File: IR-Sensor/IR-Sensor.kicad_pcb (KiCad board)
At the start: 2 copper layers, 11 parts, among them J1 Conn_01x03_Male, U1 LM324

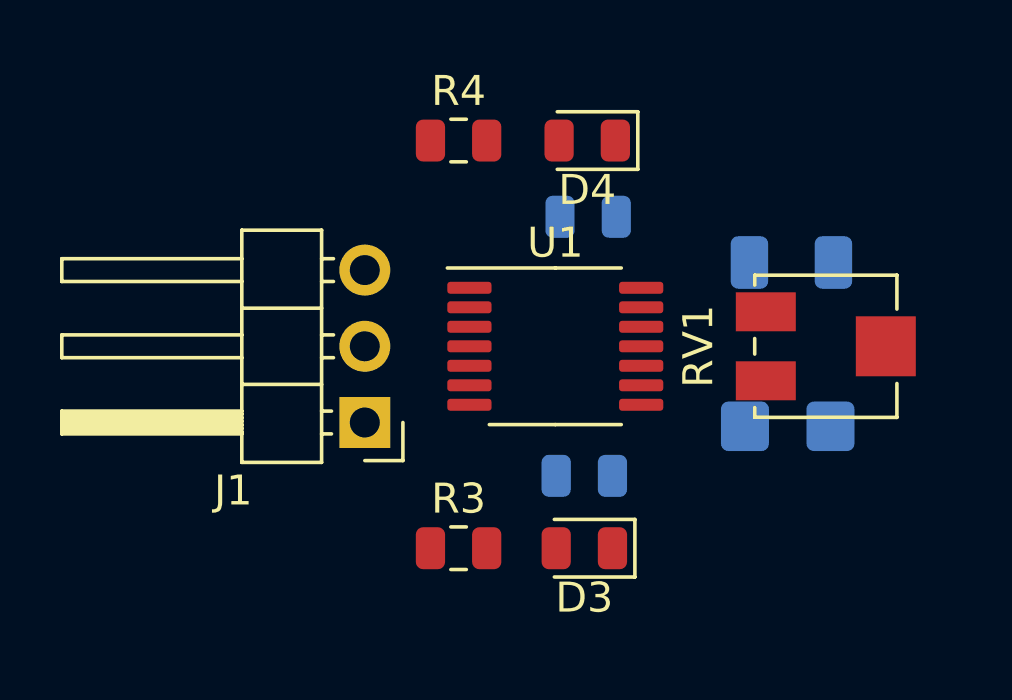
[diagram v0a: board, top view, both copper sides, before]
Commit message: Added edge cuts
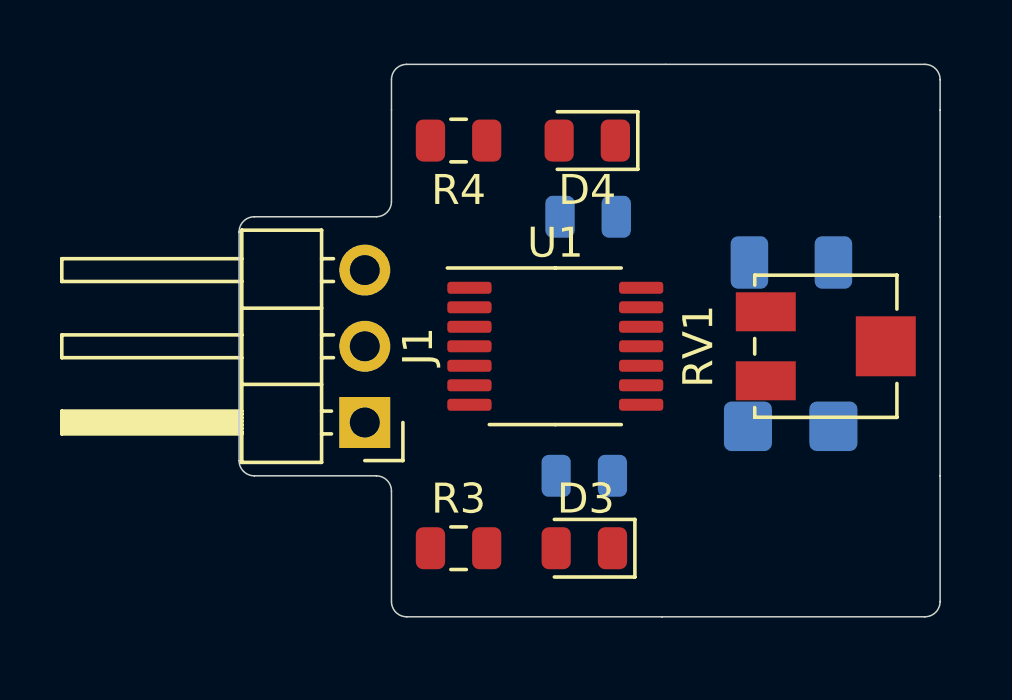
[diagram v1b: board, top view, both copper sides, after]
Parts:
- moved D2 0.10 mm to (134.3, 83.1)
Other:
- board outline added: 23.4 x 18.4 mm

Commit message: Added connections
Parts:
- turned D1 to 180 degrees
- turned D2 to 180 degrees
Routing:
- net VCC: track 0.00 -> 31.3 mm, vias 0 -> 1
- net Net-(RV1-Pad2): track 0.00 -> 19.7 mm
- net /OUTPUT: track 0.00 -> 19.6 mm, vias 0 -> 2
- net Net-(D2-Pad2): track 0.00 -> 16.8 mm, vias 0 -> 1
- net Net-(D1-Pad2): track 0.00 -> 5.07 mm
- net Net-(D4-Pad2): track 0.00 -> 2.41 mm
- net Net-(D3-Pad2): track 0.00 -> 2.32 mm
- added copper zone on B.Cu, net GND
- added copper zone on F.Cu, net GND
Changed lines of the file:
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@@
   (general
     (thickness 1.6)
-    (drawings 35)
-    (tracks 0)
+    (drawings 36)
+    (tracks 56)
     (zones 0)
     (modules 11)
@@
     (38 B.Mask user)
     (39 F.Mask user)
-    (40 Dwgs.User user)
+    (40 Dwgs.User user hide)
     (41 Cmts.User user)
     (42 Eco1.User user)
@@
   )
   (module LED_SMD:LED_1206_3216Metric (layer B.Cu)
-    (at 134.363 77.597)
+    (at 134.363 77.597 180)
     (descr "LED SMD 1206 (3216 Metric), square (rectangular) end terminal, IPC_7351 nominal, (Body size source: http://www.tortai-tech.com/upload/download/2011102023233369053.pdf), generated with kicad-footprint-generator")
     (tags diode)
@@
       (effects (font (size 0.8 0.8) (thickness 0.12)) (justify mirror))
     )
-    (pad 1 smd roundrect (at -1.4 0) (size 1.25 1.75) (layers B.Cu B.Paste B.Mask) (roundrect_rratio 0.2)
+    (pad 1 smd roundrect (at -1.4 0 180) (size 1.25 1.75) (layers B.Cu B.Paste B.Mask) (roundrect_rratio 0.2)
       (net 1 GND))
-    (pad 2 smd roundrect (at 1.4 0) (size 1.25 1.75) (layers B.Cu B.Paste B.Mask) (roundrect_rratio 0.2)
+    (pad 2 smd roundrect (at 1.4 0 180) (size 1.25 1.75) (layers B.Cu B.Paste B.Mask) (roundrect_rratio 0.2)
       (net 2 "Net-(D1-Pad2)"))
     (model ${KISYS3DMOD}/LED_SMD.3dshapes/LED_1206_3216Metric.wrl
@@
   )
   (module LED_SMD:LED_1206_3216Metric_Castellated (layer B.Cu)
-    (at 134.338 83.058)
+    (at 134.338 83.058 180)
     (descr "LED SMD 1206 (3216 Metric), castellated end terminal, IPC_7351 nominal, (Body size source: http://www.tortai-tech.com/upload/download/2011102023233369053.pdf), generated with kicad-footprint-generator")
     (tags "LED castellated")
@@
       (effects (font (size 0.8 0.8) (thickness 0.12)) (justify mirror))
     )
-    (pad 1 smd roundrect (at -1.425 0) (size 1.6 1.65) (layers B.Cu B.Paste B.Mask) (roundrect_rratio 0.15625)
+    (pad 1 smd roundrect (at -1.425 0 180) (size 1.6 1.65) (layers B.Cu B.Paste B.Mask) (roundrect_rratio 0.15625)
       (net 1 GND))
-    (pad 2 smd roundrect (at 1.425 0) (size 1.6 1.65) (layers B.Cu B.Paste B.Mask) (roundrect_rratio 0.15625)
+    (pad 2 smd roundrect (at 1.425 0 180) (size 1.6 1.65) (layers B.Cu B.Paste B.Mask) (roundrect_rratio 0.15625)
       (net 3 "Net-(D2-Pad2)"))
     (model ${KISYS3DMOD}/LED_SMD.3dshapes/LED_1206_3216Metric_Castellated.wrl
@@
   )
   (module Resistor_SMD:R_0805_2012Metric (layer B.Cu)
-    (at 127.4595 84.709)
+    (at 127.508 84.709)
     (descr "Resistor SMD 0805 (2012 Metric), square (rectangular) end terminal, IPC_7351 nominal, (Body size source: https://docs.google.com/spreadsheets/d/1BsfQQcO9C6DZCsRaXUlFlo91Tg2WpOkGARC1WS5S8t0/edit?usp=sharing), generated with kicad-footprint-generator")
     (tags resistor)
@@
     )
   )
+  (gr_line (start 131.191 83.058) (end 131.191 77.597) (layer Dwgs.User) (width 0.15))
   (gr_arc (start 138.811 71.501) (end 139.319 71.501) (angle -90) (layer Edge.Cuts) (width 0.05))
   (gr_arc (start 138.811 88.9) (end 138.811 89.408) (angle -90) (layer Edge.Cuts) (width 0.05))
@@
   (gr_line (start 123.317 87.122) (end 123.317 73.533) (layer Dwgs.User) (width 0.15))
   (gr_line (start 112.903 80.391) (end 136.271 80.391) (layer Dwgs.User) (width 0.15))
+  (segment (start 131.953 73.533) (end 132.08 73.66) (width 0.25) (layer F.Cu) (net 1))
+  (segment (start 129.667 76.073) (end 128.524 76.073) (width 0.25) (layer B.Cu) (net 2))
+  (segment (start 131.191 77.597) (end 129.667 76.073) (width 0.25) (layer B.Cu) (net 2))
+  (segment (start 132.963 77.597) (end 131.191 77.597) (width 0.25) (layer B.Cu) (net 2))
+  (segment (start 128.397 84.709) (end 129.54 84.709) (width 0.25) (layer B.Cu) (net 3))
+  (segment (start 131.191 83.058) (end 132.913 83.058) (width 0.25) (layer B.Cu) (net 3))
+  (via (at 131.064 84.201) (size 0.8) (drill 0.4) (layers F.Cu B.Cu) (net 3))
+  (segment (start 131.064 84.201) (end 130.048 84.201) (width 0.25) (layer B.Cu) (net 3))
+  (segment (start 129.54 84.709) (end 130.048 84.201) (width 0.25) (layer B.Cu) (net 3))
+  (segment (start 130.048 84.201) (end 131.191 83.058) (width 0.25) (layer B.Cu) (net 3))
+  (segment (start 125.51899 80.30699) (end 124.953 79.741) (width 0.25) (layer F.Cu) (net 3))
+  (segment (start 124.953 79.741) (end 123.6295 79.741) (width 0.25) (layer F.Cu) (net 3))
+  (segment (start 125.51899 82.5944) (end 125.51899 80.30699) (width 0.25) (layer F.Cu) (net 3))
+  (segment (start 127.12559 84.201) (end 125.51899 82.5944) (width 0.25) (layer F.Cu) (net 3))
+  (segment (start 131.064 84.201) (end 127.12559 84.201) (width 0.25) (layer F.Cu) (net 3))
+  (segment (start 124.206 87.122) (end 126.522 87.122) (width 0.25) (layer F.Cu) (net 4))
+  (segment (start 124.206 73.533) (end 126.619 73.533) (width 0.25) (layer F.Cu) (net 5))
+  (segment (start 122.892 78.441) (end 122.174 79.159) (width 0.25) (layer F.Cu) (net 6))
+  (segment (start 123.6295 78.441) (end 122.892 78.441) (width 0.25) (layer F.Cu) (net 6))
+  (segment (start 122.174 79.159) (end 122.174 79.756) (width 0.25) (layer F.Cu) (net 6))
+  (segment (start 121.539 80.391) (end 120.142 80.391) (width 0.25) (layer F.Cu) (net 6))
+  (segment (start 122.174 79.756) (end 121.539 80.391) (width 0.25) (layer F.Cu) (net 6))
+  (via (at 122.301 85.598) (size 0.8) (drill 0.4) (layers F.Cu B.Cu) (net 6))
+  (segment (start 122.331 87.122) (end 122.331 85.628) (width 0.25) (layer F.Cu) (net 6))
+  (segment (start 122.331 85.628) (end 122.301 85.598) (width 0.25) (layer F.Cu) (net 6))
+  (via (at 125.603 77.47) (size 0.8) (drill 0.4) (layers F.Cu B.Cu) (net 6))
+  (segment (start 124.968 85.598) (end 122.301 85.598) (width 0.25) (layer B.Cu) (net 6))
+  (segment (start 125.222 85.344) (end 124.968 85.598) (width 0.25) (layer B.Cu) (net 6))
+  (segment (start 124.632 78.441) (end 125.603 77.47) (width 0.25) (layer F.Cu) (net 6))
+  (segment (start 123.6295 78.441) (end 124.632 78.441) (width 0.25) (layer F.Cu) (net 6))
+  (segment (start 125.603 78.232) (end 125.222 78.613) (width 0.25) (layer B.Cu) (net 6))
+  (segment (start 125.603 77.47) (end 125.603 78.232) (width 0.25) (layer B.Cu) (net 6))
+  (segment (start 125.222 78.613) (end 125.222 85.344) (width 0.25) (layer B.Cu) (net 6))
+  (segment (start 121.793 77.851) (end 120.142 77.851) (width 0.25) (layer F.Cu) (net 7))
+  (segment (start 122.331 77.313) (end 121.793 77.851) (width 0.25) (layer F.Cu) (net 7))
+  (via (at 124.206 76.073) (size 0.8) (drill 0.4) (layers F.Cu B.Cu) (net 7))
+  (segment (start 126.649 76.073) (end 124.206 76.073) (width 0.25) (layer B.Cu) (net 7))
+  (segment (start 122.682 76.073) (end 122.331 76.424) (width 0.25) (layer F.Cu) (net 7))
+  (segment (start 124.206 76.073) (end 122.682 76.073) (width 0.25) (layer F.Cu) (net 7))
+  (segment (start 122.331 73.533) (end 122.331 76.424) (width 0.25) (layer F.Cu) (net 7))
+  (segment (start 122.331 76.424) (end 122.331 77.313) (width 0.25) (layer F.Cu) (net 7))
+  (segment (start 126.649 84.582) (end 126.522 84.709) (width 0.25) (layer B.Cu) (net 7))
+  (segment (start 133.509 79.241) (end 133.509 77.248) (width 0.25) (layer F.Cu) (net 7))
+  (segment (start 132.334 76.073) (end 124.206 76.073) (width 0.25) (layer F.Cu) (net 7))
+  (segment (start 133.509 77.248) (end 132.334 76.073) (width 0.25) (layer F.Cu) (net 7))
+  (segment (start 126.5705 76.1515) (end 126.649 76.073) (width 0.25) (layer B.Cu) (net 7))
+  (segment (start 126.5705 84.709) (end 126.5705 76.1515) (width 0.25) (layer B.Cu) (net 7))
+  (segment (start 132.423998 80.391) (end 130.81 82.004998) (width 0.25) (layer F.Cu) (net 8))
+  (segment (start 137.509 80.391) (end 132.423998 80.391) (width 0.25) (layer F.Cu) (net 8))
+  (segment (start 130.81 82.004998) (end 130.81 83.312) (width 0.25) (layer F.Cu) (net 8))
+  (segment (start 130.81 83.312) (end 130.429 83.693) (width 0.25) (layer F.Cu) (net 8))
+  (segment (start 130.429 83.693) (end 127.254 83.693) (width 0.25) (layer F.Cu) (net 8))
+  (segment (start 127.254 83.693) (end 126.238 82.677) (width 0.25) (layer F.Cu) (net 8))
+  (segment (start 126.238 82.677) (end 126.238 79.629) (width 0.25) (layer F.Cu) (net 8))
+  (segment (start 125.7 79.091) (end 123.6295 79.091) (width 0.25) (layer F.Cu) (net 8))
+  (segment (start 126.238 79.629) (end 125.7 79.091) (width 0.25) (layer F.Cu) (net 8))
+  (zone (net 1) (net_name GND) (layer B.Cu) (hatch edge 0.508)
+    (connect_pads (clearance 0.508))
+    (min_thickness 0.254)
+    (fill yes (arc_segments 32) (thermal_gap 0.508) (thermal_bridge_width 0.508))
+    (polygon
+      (pts
+        (xy 139.7 90.17) (xy 115.57 90.17) (xy 115.57 71.12) (xy 139.7 71.12)
+      )
+    )
+  )
+  (zone (net 1) (net_name GND) (layer F.Cu) (hatch edge 0.508)
+    (connect_pads (clearance 0.508))
+    (min_thickness 0.254)
+    (fill yes (arc_segments 32) (thermal_gap 0.508) (thermal_bridge_width 0.508))
+    (polygon
+      (pts
+        (xy 139.7 90.17) (xy 115.57 90.17) (xy 115.57 71.12) (xy 139.7 71.12)
+      )
+    )
+  )
 )

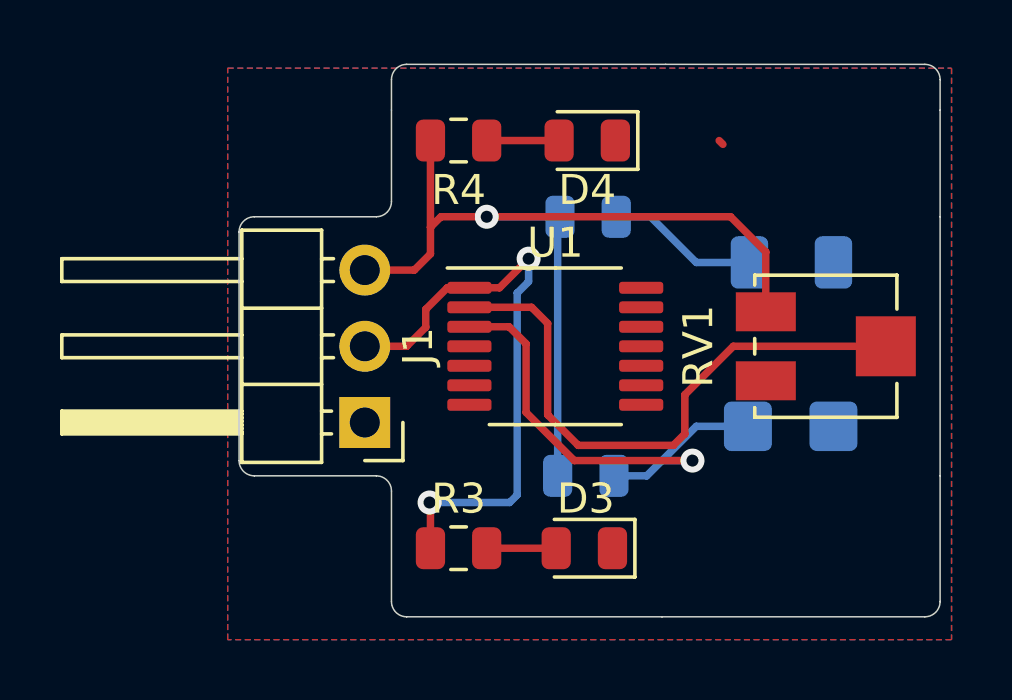
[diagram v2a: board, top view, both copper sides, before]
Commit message: Added text skillscreen
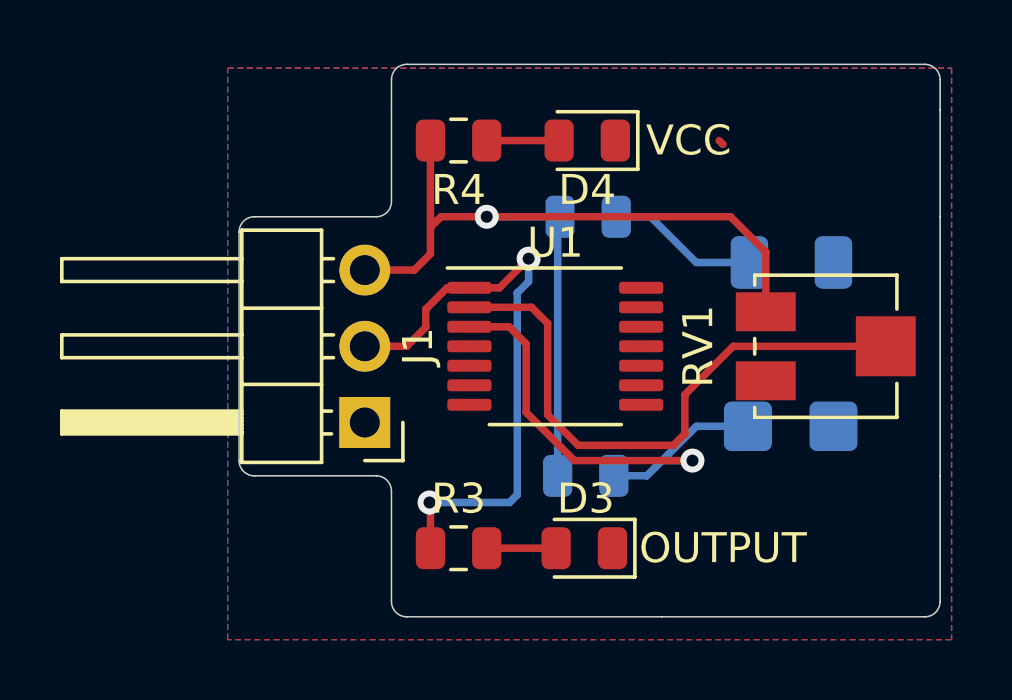
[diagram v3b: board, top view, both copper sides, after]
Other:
- board text added: "OUTPUT"
- board text added: "RX"
- board text added: "TX"
- board text added: "VCC"
- board text added: "VCC OUTPUT GND"
